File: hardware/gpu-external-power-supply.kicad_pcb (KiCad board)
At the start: 2 copper layers, 11 x 14 mm, 9 parts, among them SW7001 SW_Wuerth_450301014042, SW8001 CK_KMS2xxG, SW8002 CK_KMS2xxG, SW8003 CK_KMS2xxG, SW8004 CK_KMS2xxG, SW8005 CK_KMS2xxG, U4001 ACS758xCB-150B-PSS, U5001 LD1117S33TR_SOT223, U7001 STM32C031K6Tx

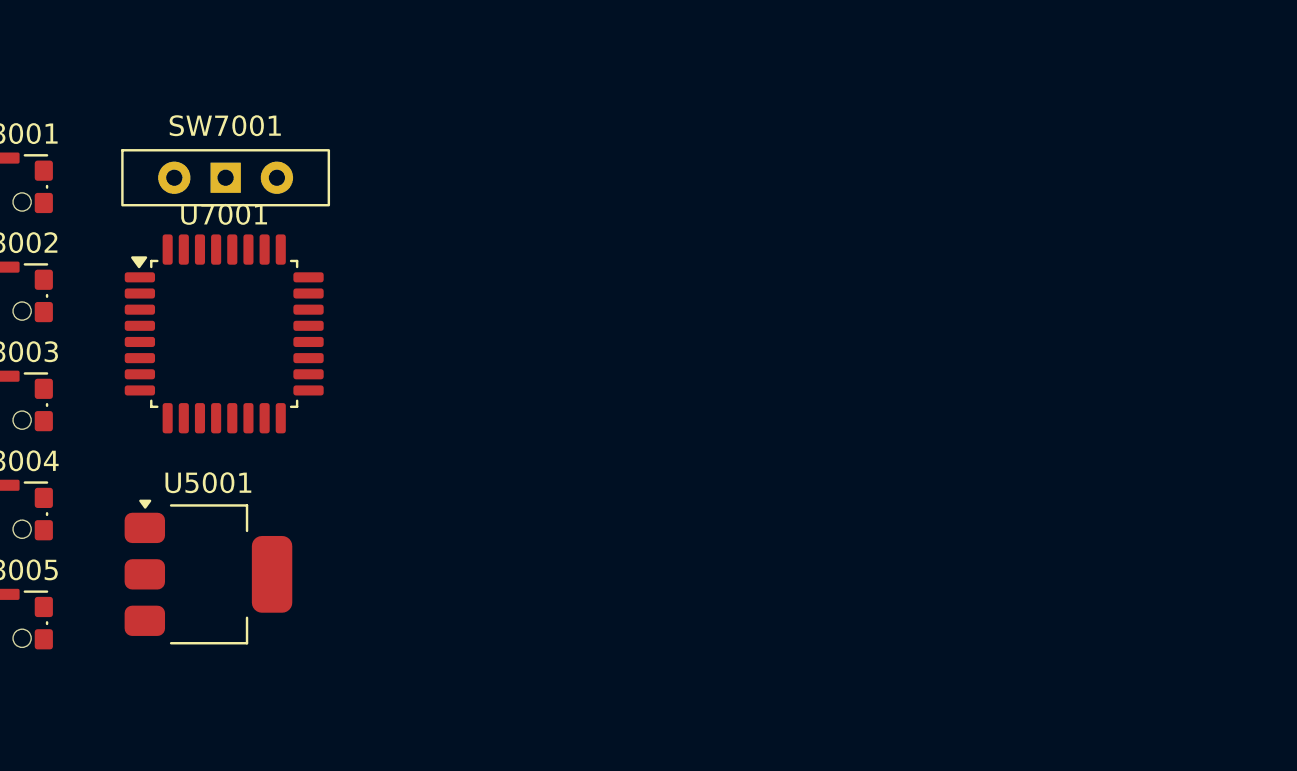
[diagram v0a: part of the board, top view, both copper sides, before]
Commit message: feat(pcb): add manufacturing constraints
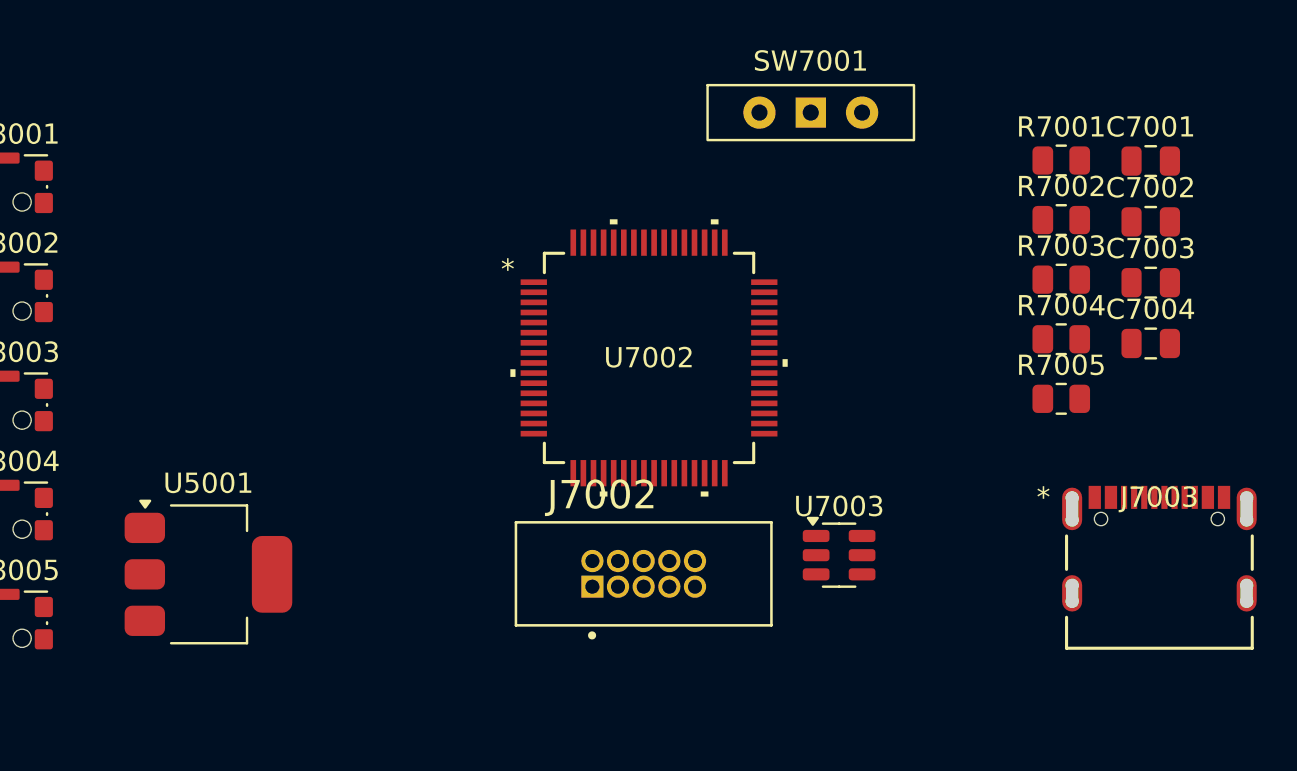
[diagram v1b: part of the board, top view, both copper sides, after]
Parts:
- removed U7001: STM32C031K6Tx, Package_QFP:LQFP-32_7x7mm_P0.8mm
- added C7001: 6pF, Capacitor_SMD:C_0805_2012Metric, F.Cu at (197.2, 90.0)
- added C7002: 6pF, Capacitor_SMD:C_0805_2012Metric, F.Cu at (197.2, 93.0)
- added C7003: 4.7u, Capacitor_SMD:C_0805_2012Metric, F.Cu at (197.2, 96.0)
- added C7004: 100n, Capacitor_SMD:C_0805_2012Metric, F.Cu at (197.2, 99.1)
- added J7002: Conn_ARM_JTAG_SWD_10, work:CNC_3221-10-0100-00, F.Cu at (172.1, 110.5)
- added J7003: USB_C_Receptacle_USB2.0_16P, work:12402012E212A_AMP, F.Cu at (197.6, 110.4)
- added R7001: 5K1, Resistor_SMD:R_0805_2012Metric, F.Cu at (192.7, 90.0)
- added R7002: 5K1, Resistor_SMD:R_0805_2012Metric, F.Cu at (192.7, 93.0)
- added R7003: 10K, Resistor_SMD:R_0805_2012Metric, F.Cu at (192.7, 95.9)
- added R7004: 100k, Resistor_SMD:R_0805_2012Metric, F.Cu at (192.7, 98.8)
- added R7005: 100k, Resistor_SMD:R_0805_2012Metric, F.Cu at (192.7, 101.8)
- added U7002: STM32C071RBT6, work:LQFP-64_STM, F.Cu at (172.3, 99.8)
- added U7003: USBLC6-2SC6, Package_TO_SOT_SMD:SOT-23-6, F.Cu at (181.7, 109.5)
- moved SW7001 29.1 mm to (180.3, 87.6)
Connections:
- SW7001 pad 1: BOOT0 -> SWCLK
- SW7001 pad 2: unconnected-(SW7001-C-Pad2) -> GND
- SW8001 pad 2: unconnected-(SW8001-Pad2) -> OB_LEFT
- SW8001 pad SH: Net-(SW8001-B) -> GND
- SW8002 pad 2: unconnected-(SW8002-Pad2) -> OB_UP
- SW8002 pad SH: Net-(SW8001-B) -> GND
- SW8003 pad 2: unconnected-(SW8003-Pad2) -> OB_ENTER
- SW8003 pad SH: Net-(SW8001-B) -> GND
- SW8004 pad 1: /Onboard Control/b2 -> OB_DOWN
- SW8004 pad SH: Net-(SW8001-B) -> GND
- SW8005 pad 2: unconnected-(SW8005-Pad2) -> OB_RIGHT
- SW8005 pad SH: Net-(SW8001-B) -> GND
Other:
- copper layers 2 -> 6

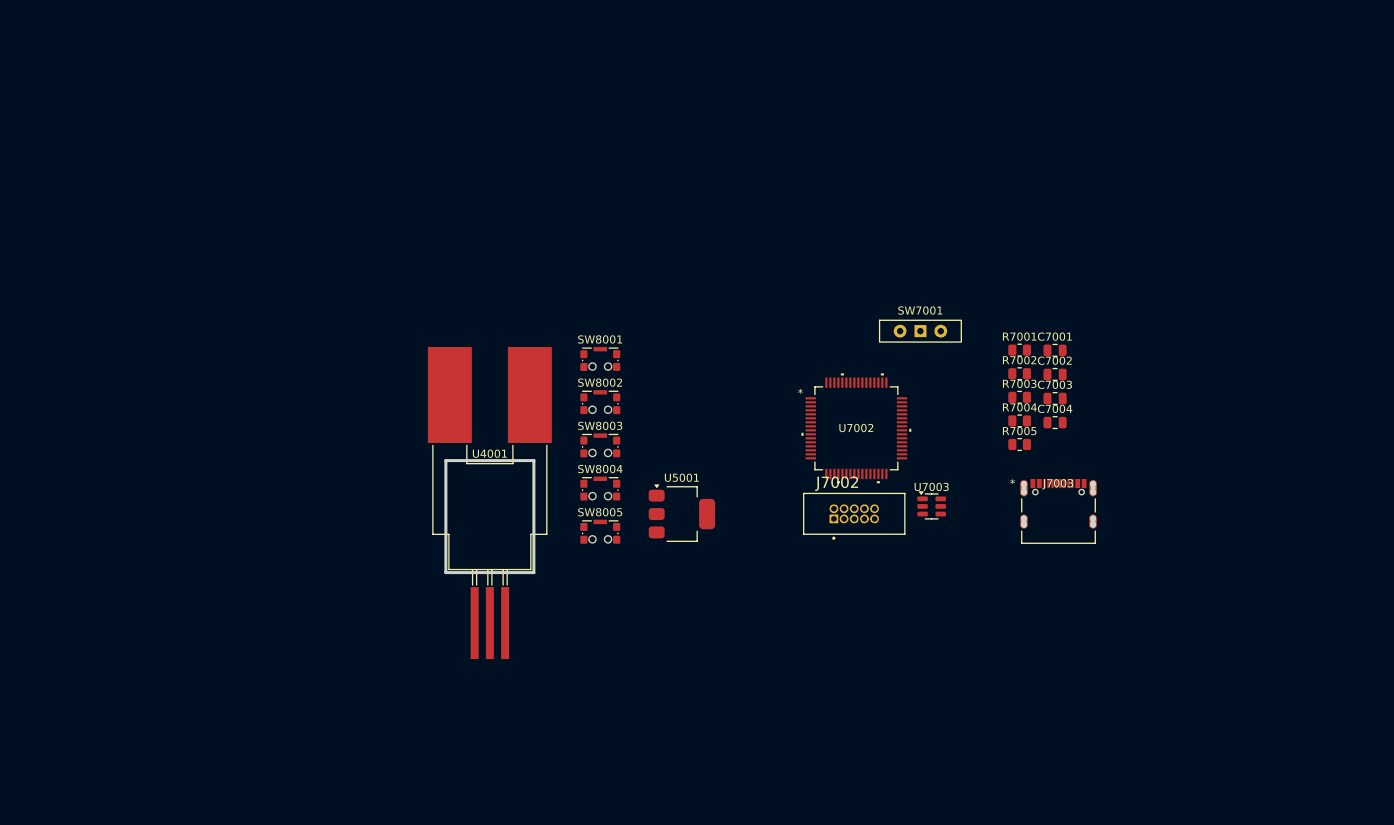
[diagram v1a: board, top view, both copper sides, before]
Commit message: feat(pcb): onboard control grid
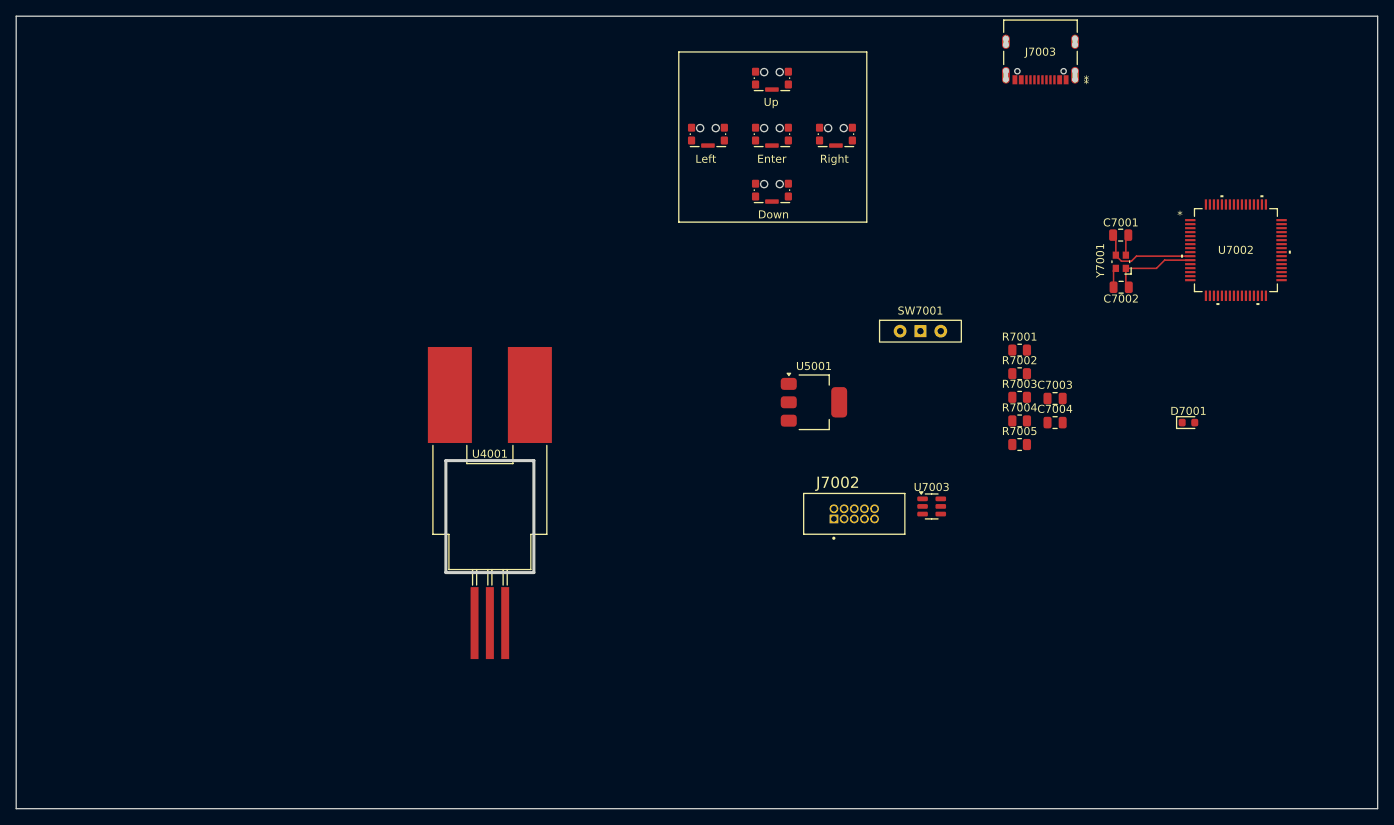
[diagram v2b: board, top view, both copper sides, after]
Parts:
- added D7001: GG060303100N2P, Diode_SMD:D_0603_1608Metric, F.Cu at (213.8, 99.1)
- added Y7001: Crystal_GND24, Crystal:Crystal_SMD_Abracon_ABM10-4Pin_2.5x2.0mm, F.Cu at (205.4, 79.0)
- moved SW8005 58.0 mm to (169.8, 63.0), turned to 180 degrees
- moved J7003 57.9 mm to (195.3, 52.5), turned to 180 degrees
- moved U7002 52.4 mm to (219.8, 77.5)
- moved SW8002 46.0 mm to (161.8, 56.0), turned to 180 degrees
- moved SW8003 44.6 mm to (161.8, 63.0), turned to 180 degrees
- moved SW8004 43.2 mm to (161.8, 70.0), turned to 180 degrees
- moved SW8001 31.3 mm to (153.8, 63.0), turned to 180 degrees
- moved U5001 21.6 mm to (167.0, 96.5)
- moved C7001 16.6 mm to (205.4, 75.6), turned to 180 degrees
- moved C7002 13.7 mm to (205.4, 82.1)
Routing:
- net /U Controller/PF0: track 0.00 -> 12.5 mm
- net /U Controller/PF1: track 0.00 -> 11.0 mm
- net GND: track 0.00 -> 5.11 mm
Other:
- board size 11 x 14 mm -> 170.2 x 99.1 mm
- board text added: "Down"
- board text added: "Enter"
- board text added: "Left"
- board text added: "Right"
- board text added: "Up"

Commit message: feat(pcb): microcontroller and onboard control initial design
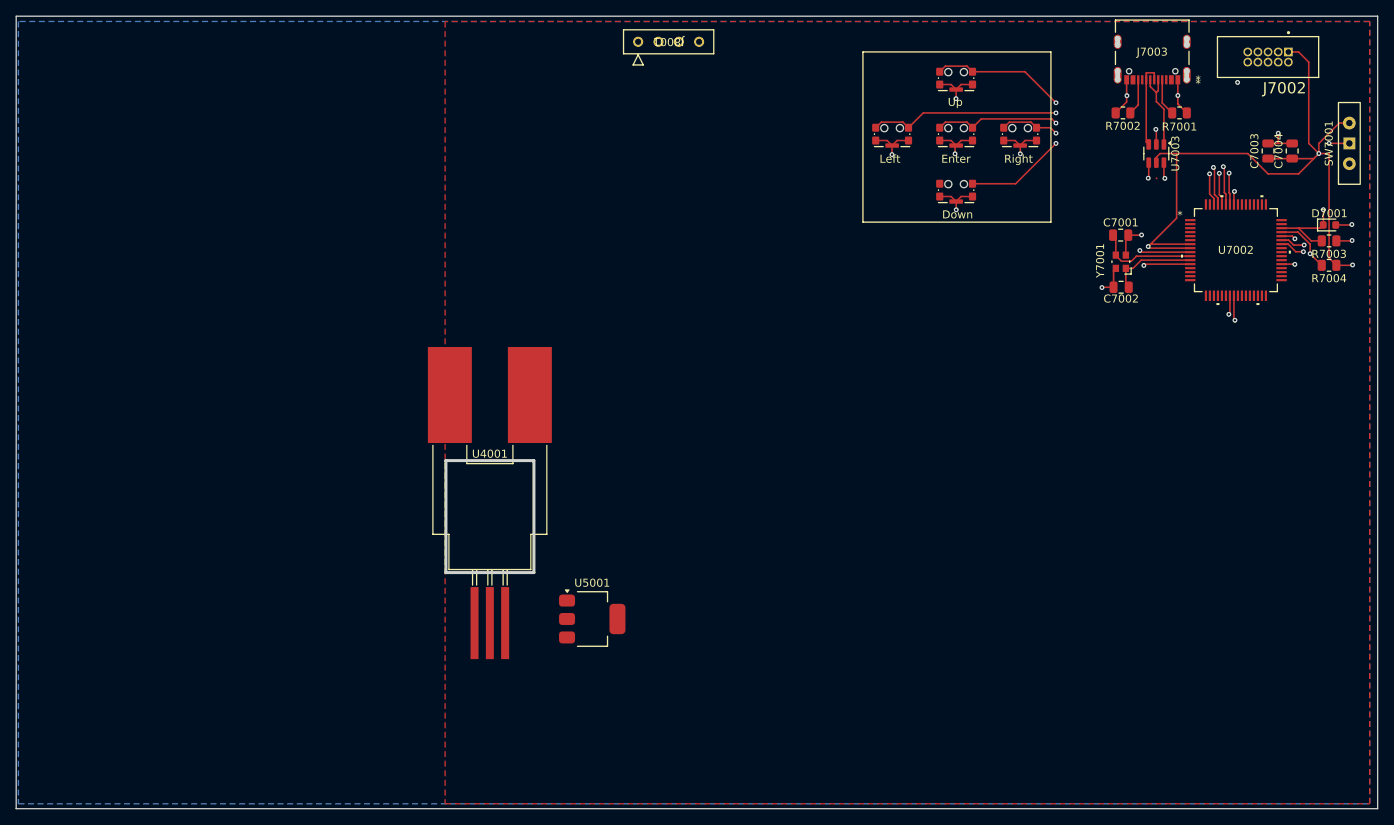
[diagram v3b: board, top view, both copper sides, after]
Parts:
- removed R7005: 100k, Resistor_SMD:R_0805_2012Metric
- added J8001: Conn_01x04_Pin, work:CONN_PPTC041LFBN-RC_SUL, F.Cu at (145.1, 51.5)
- moved J7002 77.0 mm to (223.8, 53.4), turned to 180 degrees
- moved SW7001 58.5 mm to (234.0, 64.2), turned to 90 degrees
- moved U7003 52.3 mm to (209.8, 65.4), turned to -90 degrees
- moved C7004 45.1 mm to (226.8, 65.1), turned to 90 degrees
- moved R7003 43.3 mm to (231.4, 76.3), turned to 180 degrees
- moved R7004 43.3 mm to (231.4, 79.4), turned to 180 degrees
- moved C7003 40.8 mm to (223.8, 65.1), turned to 90 degrees
- moved U5001 38.8 mm to (139.3, 123.6)
- moved R7001 35.8 mm to (212.7, 60.4)
- moved R7002 35.1 mm to (205.7, 60.4), turned to 180 degrees
- moved D7001 30.3 mm to (231.5, 74.4)
- moved SW8001 23.0 mm to (176.8, 63.0)
- moved SW8002 23.0 mm to (184.8, 56.0)
- moved SW8003 23.0 mm to (184.8, 63.0)
- moved SW8004 23.0 mm to (184.8, 70.0)
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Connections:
- net VDD renamed 3.3V
- SW8004 pad 1: OB_DOWN -> GND
- SW8004 pad 2: GND -> OB_DOWN
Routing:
- net 3.3V: track 0.00 -> 91.6 mm, vias 0 -> 3
- net I2C_SCL: track 0.00 -> 87.1 mm, vias 0 -> 1
- net I2C_SDA: track 0.00 -> 82.7 mm, vias 0 -> 1
- net GND: track 5.11 -> 62.7 mm, vias 0 -> 14
- net OB_LEFT: track 0.00 -> 51.9 mm, vias 0 -> 2
- net OB_UP: track 0.00 -> 46.5 mm, vias 0 -> 2
- net OB_DOWN: track 0.00 -> 44.6 mm, vias 0 -> 2
- net OB_ENTER: track 0.00 -> 41.7 mm, vias 0 -> 2
- net NRST: track 0.00 -> 39.7 mm, vias 0 -> 1
- net SWCLK: track 0.00 -> 34.2 mm, vias 0 -> 2
- net OB_RIGHT: track 0.00 -> 33.7 mm, vias 0 -> 2
- net SWDIO: track 0.00 -> 33.0 mm, vias 0 -> 1
- net USB_DN: track 0.00 -> 29.6 mm, vias 0 -> 2
- net USB_DP: track 0.00 -> 28.8 mm, vias 0 -> 2
- net SWO: track 0.00 -> 20.3 mm, vias 0 -> 2
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- added copper zone on F.Cu, net /12V Supply/12v_spply_lw_crrnt_spply_dcpwr
- added copper zone on B.Cu, net GND
- added copper zone on In1.Cu, net GND
- added copper zone on In3.Cu, net GND

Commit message: feat(PCB): 12V supply layout
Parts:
- removed U4001: ACS758xCB-150B-PSS, Sensor_Current:Allegro_CB_PSS
- added C1: 100pF, Capacitor_SMD:C_0805_2012Metric, F.Cu at (380.6, 148.9)
- added C10: 1nF, Capacitor_SMD:C_0805_2012Metric, F.Cu at (389.5, 151.9)
- added C11: 1nF, Capacitor_SMD:C_0805_2012Metric, F.Cu at (389.5, 154.9)
- added C12: 0.1uF, Capacitor_SMD:C_0805_2012Metric, F.Cu at (389.5, 157.9)
- added C2: 100pF, Capacitor_SMD:C_0805_2012Metric, F.Cu at (380.6, 151.9)
- added C3: 2200pF, Capacitor_SMD:C_0805_2012Metric, F.Cu at (380.6, 154.9)
- added C4: 1uF, Capacitor_SMD:C_0805_2012Metric, F.Cu at (380.6, 157.9)
- added C4001: 470u, Capacitor_SMD:C_0805_2012Metric, F.Cu at (212.1, 125.9)
- added C4002: 470u, Capacitor_SMD:C_0805_2012Metric, F.Cu at (213.9, 108.8)
- added C4003: 470u, Capacitor_SMD:C_0805_2012Metric, F.Cu at (211.6, 90.8)
- added C4004: 47u, Capacitor_SMD:C_0805_2012Metric, F.Cu at (209.3, 125.9)
- added C4005: 47u, Capacitor_SMD:C_0805_2012Metric, F.Cu at (211.1, 108.8)
- added C4006: 47u, Capacitor_SMD:C_0805_2012Metric, F.Cu at (208.7, 90.8)
- added C4007: 10u, Capacitor_SMD:C_0805_2012Metric, F.Cu at (209.6, 138.1)
- added C4008: 10u, Capacitor_SMD:C_0805_2012Metric, F.Cu at (209.2, 122.3)
- added C4009: 10u, Capacitor_SMD:C_0805_2012Metric, F.Cu at (211.0, 104.9)
- added C4010: 0.1u, Capacitor_SMD:C_0805_2012Metric, F.Cu at (212.4, 138.1)
- added C4011: 0.1u, Capacitor_SMD:C_0805_2012Metric, F.Cu at (212.1, 122.3)
- added C4012: 0.1u, Capacitor_SMD:C_0805_2012Metric, F.Cu at (213.9, 104.9)
- added C4013: 330u, Capacitor_SMD:C_0805_2012Metric, F.Cu at (204.8, 104.3)
- added C4014: 330u, Capacitor_SMD:C_0805_2012Metric, F.Cu at (204.8, 120.6)
- added C4015: 330u, Capacitor_SMD:C_0805_2012Metric, F.Cu at (204.9, 137.5)
- added C4016: 470u, Capacitor_THT:CP_Radial_D8.0mm_P3.50mm, F.Cu at (197.1, 98.1)
- added C4017: 470u, Capacitor_THT:CP_Radial_D8.0mm_P3.50mm, F.Cu at (197.6, 113.3)
- added C4018: 470u, Capacitor_THT:CP_Radial_D8.0mm_P3.50mm, F.Cu at (197.4, 130.3)
- added C4021: 0.1u, Capacitor_SMD:C_0805_2012Metric, F.Cu at (200.2, 85.7)
- added C5: 4.7uF, Capacitor_SMD:C_0805_2012Metric, F.Cu at (385.0, 148.9)
- added C5001: 10uF, Capacitor_SMD:C_0805_2012Metric_Pad1.18x1.45mm_HandSolder, F.Cu at (169.0, 84.0)
- added C5002: 22uF, Capacitor_SMD:C_0805_2012Metric, F.Cu at (170.4, 80.6)
- added C5003: 1uF, Capacitor_SMD:C_0805_2012Metric, F.Cu at (184.7, 84.8)
- added C5004: 1uF, Capacitor_SMD:C_0805_2012Metric, F.Cu at (188.3, 81.4)
- added C6: 2200pF, Capacitor_SMD:C_0805_2012Metric, F.Cu at (385.0, 151.9)
- added C7: 1uF, Capacitor_SMD:C_0805_2012Metric, F.Cu at (385.0, 154.9)
- added C8: 1uF, Capacitor_SMD:C_0805_2012Metric, F.Cu at (385.0, 157.9)
- added C9: 1uF, Capacitor_SMD:C_0805_2012Metric, F.Cu at (389.5, 148.9)
- added D4001: 150080SS75000, LED_SMD:LED_0805_2012Metric_Pad1.15x1.40mm_HandSolder, F.Cu at (208.7, 144.4)
- added D5001: 150080SS75000, LED_SMD:LED_0805_2012Metric_Pad1.15x1.40mm_HandSolder, F.Cu at (189.8, 90.1)
- added D5002: 150080SS75000, LED_SMD:LED_0805_2012Metric_Pad1.15x1.40mm_HandSolder, F.Cu at (193.8, 89.2)
- added J4001: 353180620, 2x3_PCIe_Conn:CONN_35318-06xx_MOL, F.Cu at (222.3, 127.1)
- added J4002: 353180620, 2x3_PCIe_Conn:CONN_35318-06xx_MOL, F.Cu at (222.3, 110.6)
- added J4004: 353180620, 2x3_PCIe_Conn:CONN_35318-06xx_MOL, F.Cu at (222.3, 94.1)
- added L4001: 170nH, 170nH_SMD_Ind:IND_IFLR4031GCERR17M01_VIS-L, F.Cu at (207.9, 131.9)
- added L4002: 170nH, 170nH_SMD_Ind:IND_IFLR4031GCERR17M01_VIS-L, F.Cu at (207.9, 115.0)
- added L4003: 170nH, 170nH_SMD_Ind:IND_IFLR4031GCERR17M01_VIS-L, F.Cu at (207.9, 98.7)
- added L5001: 2.2uH, Inductor_SMD:L_0805_2012Metric_Pad1.15x1.40mm_HandSolder, F.Cu at (174.6, 82.0)
- added R1: 130k, Resistor_SMD:R_0805_2012Metric, F.Cu at (380.6, 134.1)
- added R10: 10k, Resistor_SMD:R_0805_2012Metric, F.Cu at (385.0, 134.1)
- added R11: 10k, Resistor_SMD:R_0805_2012Metric, F.Cu at (385.0, 137.1)
- added R12: 10k, Resistor_SMD:R_0805_2012Metric, F.Cu at (385.0, 140.0)
- added R13: 10k, Resistor_SMD:R_0805_2012Metric, F.Cu at (385.0, 143.0)
- added R14: 10k, Resistor_SMD:R_0805_2012Metric, F.Cu at (385.0, 145.9)
- added R15: 10k, Resistor_SMD:R_0805_2012Metric, F.Cu at (389.4, 134.1)
- added R16: 10k, Resistor_SMD:R_0805_2012Metric, F.Cu at (389.4, 137.1)
- added R17: 10k, Resistor_SMD:R_0805_2012Metric, F.Cu at (389.4, 140.0)
- added R18: 10k, Resistor_SMD:R_0805_2012Metric, F.Cu at (389.4, 143.0)
- added R19: 1m, Resistor_SMD:R_Shunt_Vishay_WSK2512_6332Metric_T1.19mm, F.Cu at (4.41, 1.93)
- added R2: 2430k, Resistor_SMD:R_0805_2012Metric, F.Cu at (380.6, 137.1)
- added R20: 1m, Resistor_SMD:R_Shunt_Vishay_WSK2512_6332Metric_T1.19mm, F.Cu at (4.41, 6.78)
- added R3: 37.4k, Resistor_SMD:R_0805_2012Metric, F.Cu at (380.6, 140.0)
- added R4: 37.4k, Resistor_SMD:R_0805_2012Metric, F.Cu at (380.6, 143.0)
- added R4001: 337, Resistor_SMD:R_0805_2012Metric, F.Cu at (205.3, 143.3)
- added R4002: 10k, Resistor_SMD:R_0805_2012Metric, F.Cu at (204.7, 89.2)
- added R4003: 3.5k, Resistor_SMD:R_0805_2012Metric, F.Cu at (202.2, 85.7)
- added R5: 0, Resistor_SMD:R_2512_6332Metric_Pad1.40x3.35mm_HandSolder, F.Cu at (373.8, 135.1)
- added R5001: 100k, Resistor_SMD:R_0805_2012Metric, F.Cu at (176.2, 85.2)
- added R5002: 100+-5, Resistor_SMD:R_0805_2012Metric, F.Cu at (185.0, 90.1)
- added R5003: 1, Resistor_SMD:R_0805_2012Metric, F.Cu at (180.9, 79.8)
- added R5004: 45+-5, Resistor_SMD:R_0805_2012Metric, F.Cu at (193.8, 85.1)
- added R5005: 1, Resistor_SMD:R_0805_2012Metric, F.Cu at (194.9, 80.6)
- added R6: 0, Resistor_SMD:R_2512_6332Metric_Pad1.40x3.35mm_HandSolder, F.Cu at (373.9, 140.3)
- added R7: 0, Resistor_SMD:R_2512_6332Metric_Pad1.40x3.35mm_HandSolder, F.Cu at (373.8, 144.9)
- added R8: 0, Resistor_SMD:R_2512_6332Metric_Pad1.40x3.35mm_HandSolder, F.Cu at (373.8, 149.8)
- added R9: 10k, Resistor_SMD:R_0805_2012Metric, F.Cu at (380.6, 145.9)
- added TP5001: 12V -> 5V, TestPoint:TestPoint_Pad_1.5x1.5mm, F.Cu at (169.0, 90.1)
- added TP5003: TestPoint, TestPoint:TestPoint_Pad_1.5x1.5mm, F.Cu at (176.3, 77.2)
- added TP5004: TestPoint, TestPoint:TestPoint_Pad_1.5x1.5mm, F.Cu at (185.3, 77.4)
- added TP5005: TestPoint, TestPoint:TestPoint_Pad_1.5x1.5mm, F.Cu at (192.3, 77.8)
- added TP5006: TestPoint, TestPoint:TestPoint_Pad_1.5x1.5mm, F.Cu at (197.5, 77.8)
- added U5002: TPS73633DBVR, TPS73633DBVR_SOT23-5:DBV5, F.Cu at (188.3, 84.8)
- U5001: value LD1117S33TR_SOT223 -> TPS62160DSG; footprint Package_TO_SOT_SMD:SOT-223-3_TabPin2 -> Package_SON:WSON-8-1EP_2x2mm_P0.5mm_EP0.9x1.6mm_ThermalVias
- moved U5001 51.2 mm to (172.8, 84.9)
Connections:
- U5001 pad 2: /Low Current Supply/lw_crrnt_spply_u_cntrllr_dcpwr -> /Low Current Supply/12v_spply_lw_crrnt_spply_dcpwr
- U7002 pad 18: 12V_VOL_SENS -> PMBUS_SMBA
- U7002 pad 19: unconnected-(U7002-PA2-Pad19) -> 12V_VOL_SENS
- U7002 pad 38: unconnected-(U7002-PC6-Pad38) -> AVR_READY
- U7002 pad 39: unconnected-(U7002-PC7-Pad39) -> BVR_READY
- U7002 pad 48: unconnected-(U7002-PC8-Pad48) -> VR_FAULT
- U7002 pad 49: unconnected-(U7002-PC9-Pad49) -> A_ENABLE
- U7002 pad 64: unconnected-(U7002-PC10-Pad64) -> B_ENABLE
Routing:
- net GND: track 62.7 -> 113.1 mm, vias 14 -> 30
- net 12V_VOL_SENS: track 0.00 -> 20.2 mm
- net Net-(D4001-A): track 0.00 -> 2.42 mm
- added copper zone on F.Cu, net 12V
- added copper zone on F.Cu, net Net-(C4001-Pad1)
- added copper zone on F.Cu, net Net-(C4002-Pad1)
- added copper zone on F.Cu, net Net-(C4003-Pad1)
- removed copper zone on F.Cu, net /12V Supply/12v_spply_lw_crrnt_spply_dcpwr
